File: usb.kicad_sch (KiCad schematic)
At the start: 20 parts, among them J1 USB_B, J3 USB_B, U7 USB3320C-EZK

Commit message: removed all resistors 0201mm, changed to 0402mm
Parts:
- R28: footprint Resistor_SMD:R_0201_0603Metric -> Resistor_SMD:R_0402_1005Metric
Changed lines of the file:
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@@
 			)
 		)
-		(property "Footprint" "Resistor_SMD:R_0201_0603Metric"
+		(property "Footprint" "Resistor_SMD:R_0402_1005Metric"
 			(at 110.49 77.978 90)
 			(effects

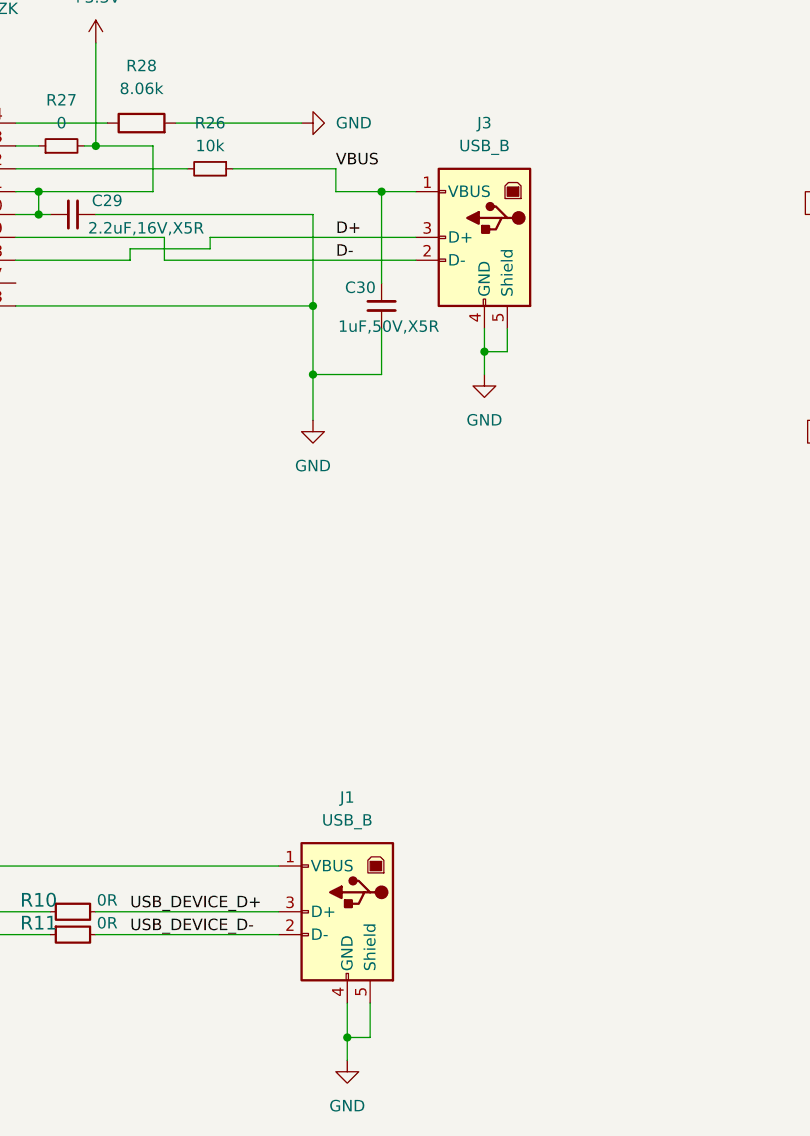
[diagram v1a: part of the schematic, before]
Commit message: moved to 6 layers, fixing DRC issues
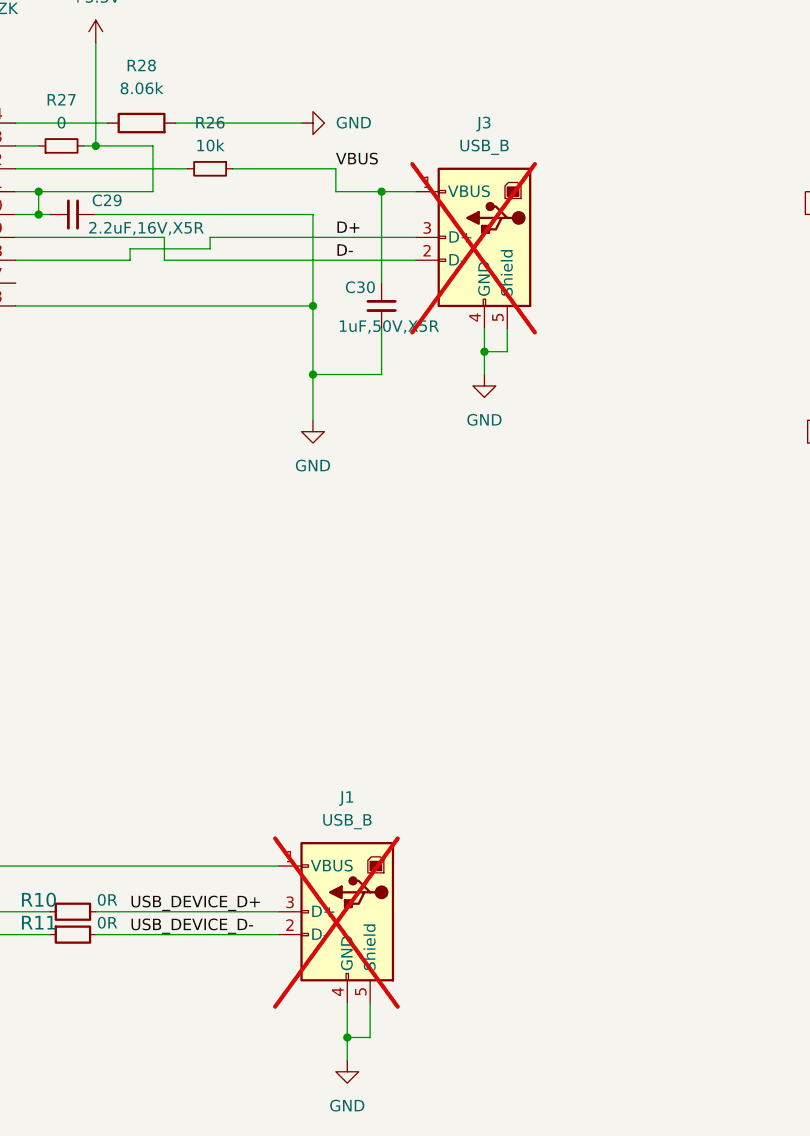
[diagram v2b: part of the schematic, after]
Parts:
- J1, J3: now not fitted
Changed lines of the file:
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@@
 		(in_bom yes)
 		(on_board yes)
-		(dnp no)
+		(dnp yes)
 		(property "Reference" "J3"
 			(at 148.59 76.2 0)
@@
 		(in_bom yes)
 		(on_board yes)
-		(dnp no)
+		(dnp yes)
 		(property "Reference" "J1"
 			(at 133.35 151.13 0)
